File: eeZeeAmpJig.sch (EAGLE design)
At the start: 19 parts

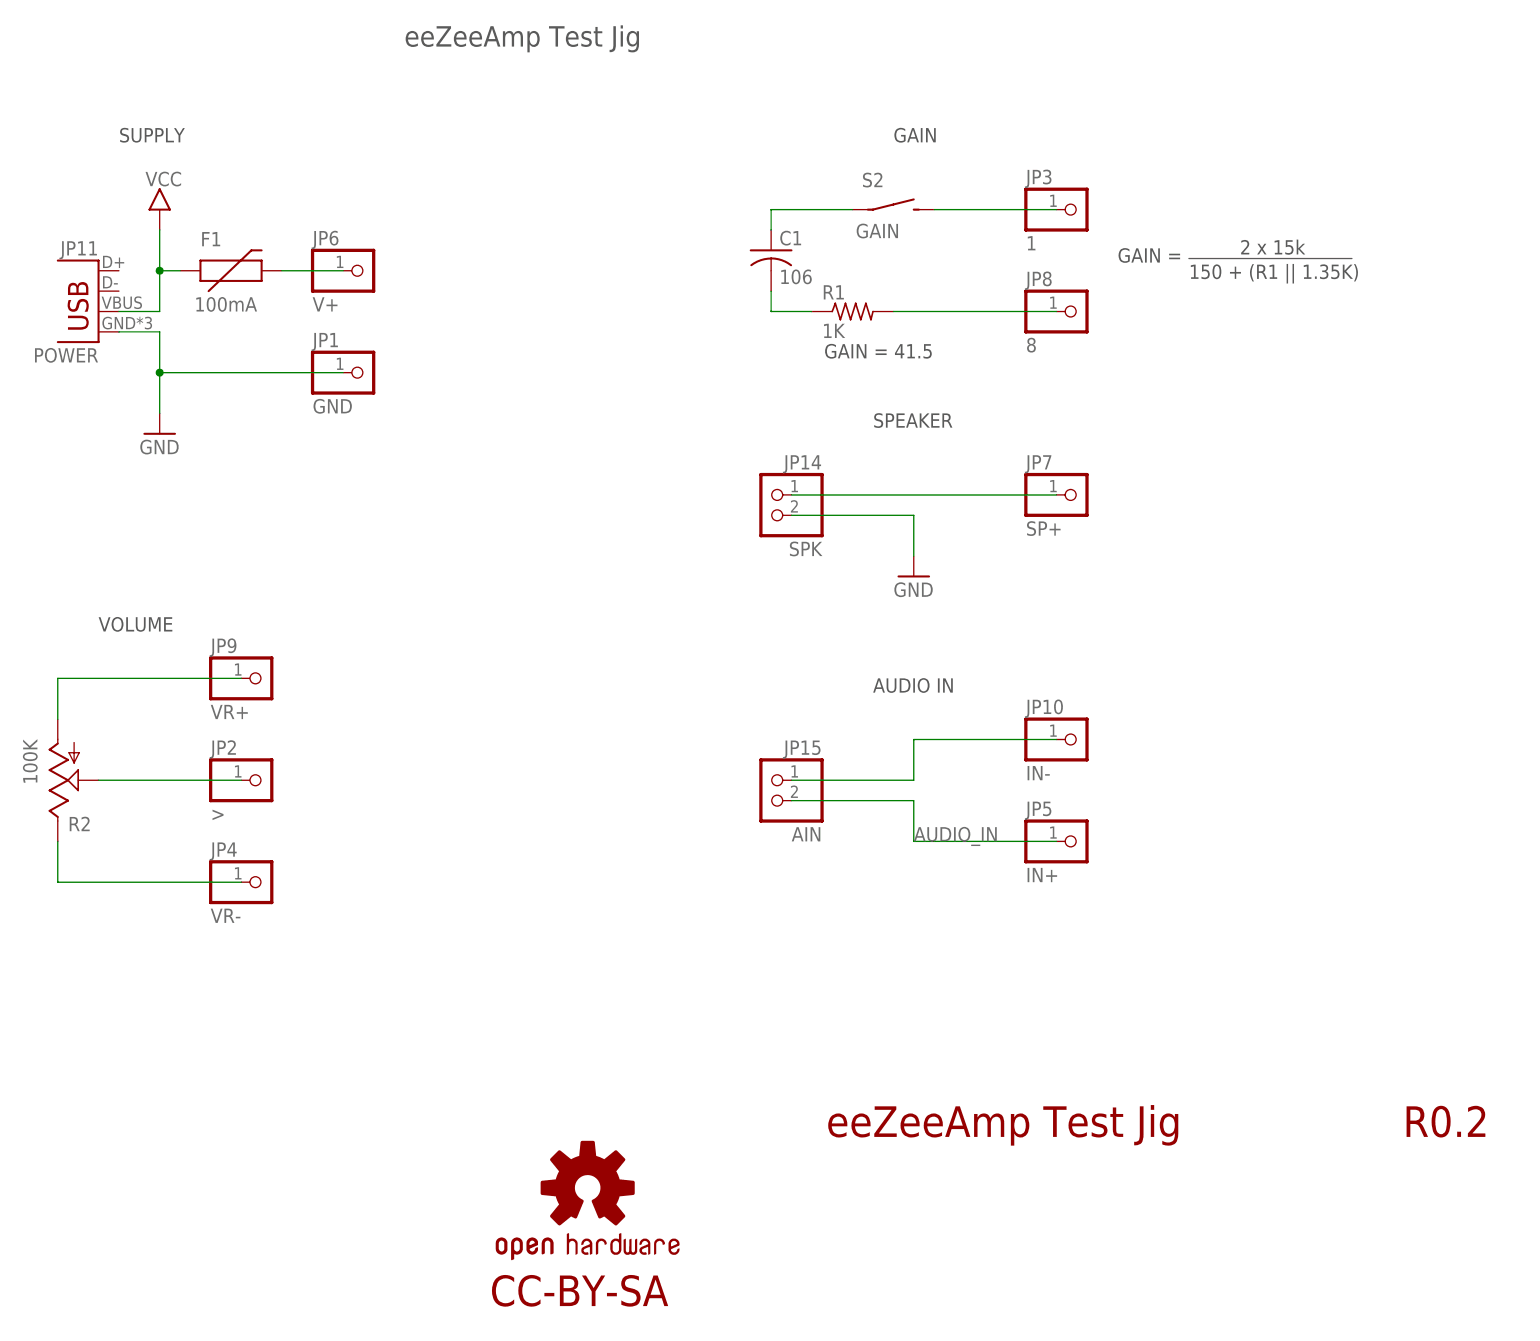
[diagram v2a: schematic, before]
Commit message: increased drill size for pogos, replaced microB with pin headers, moved power, ain, spkr pin headers, shrank board, centered pogo pin test area, reduced mounting hole drill size to #2, reduced spacer tdocu circles to actual for #2 size screws, changed switch to smaller smt version
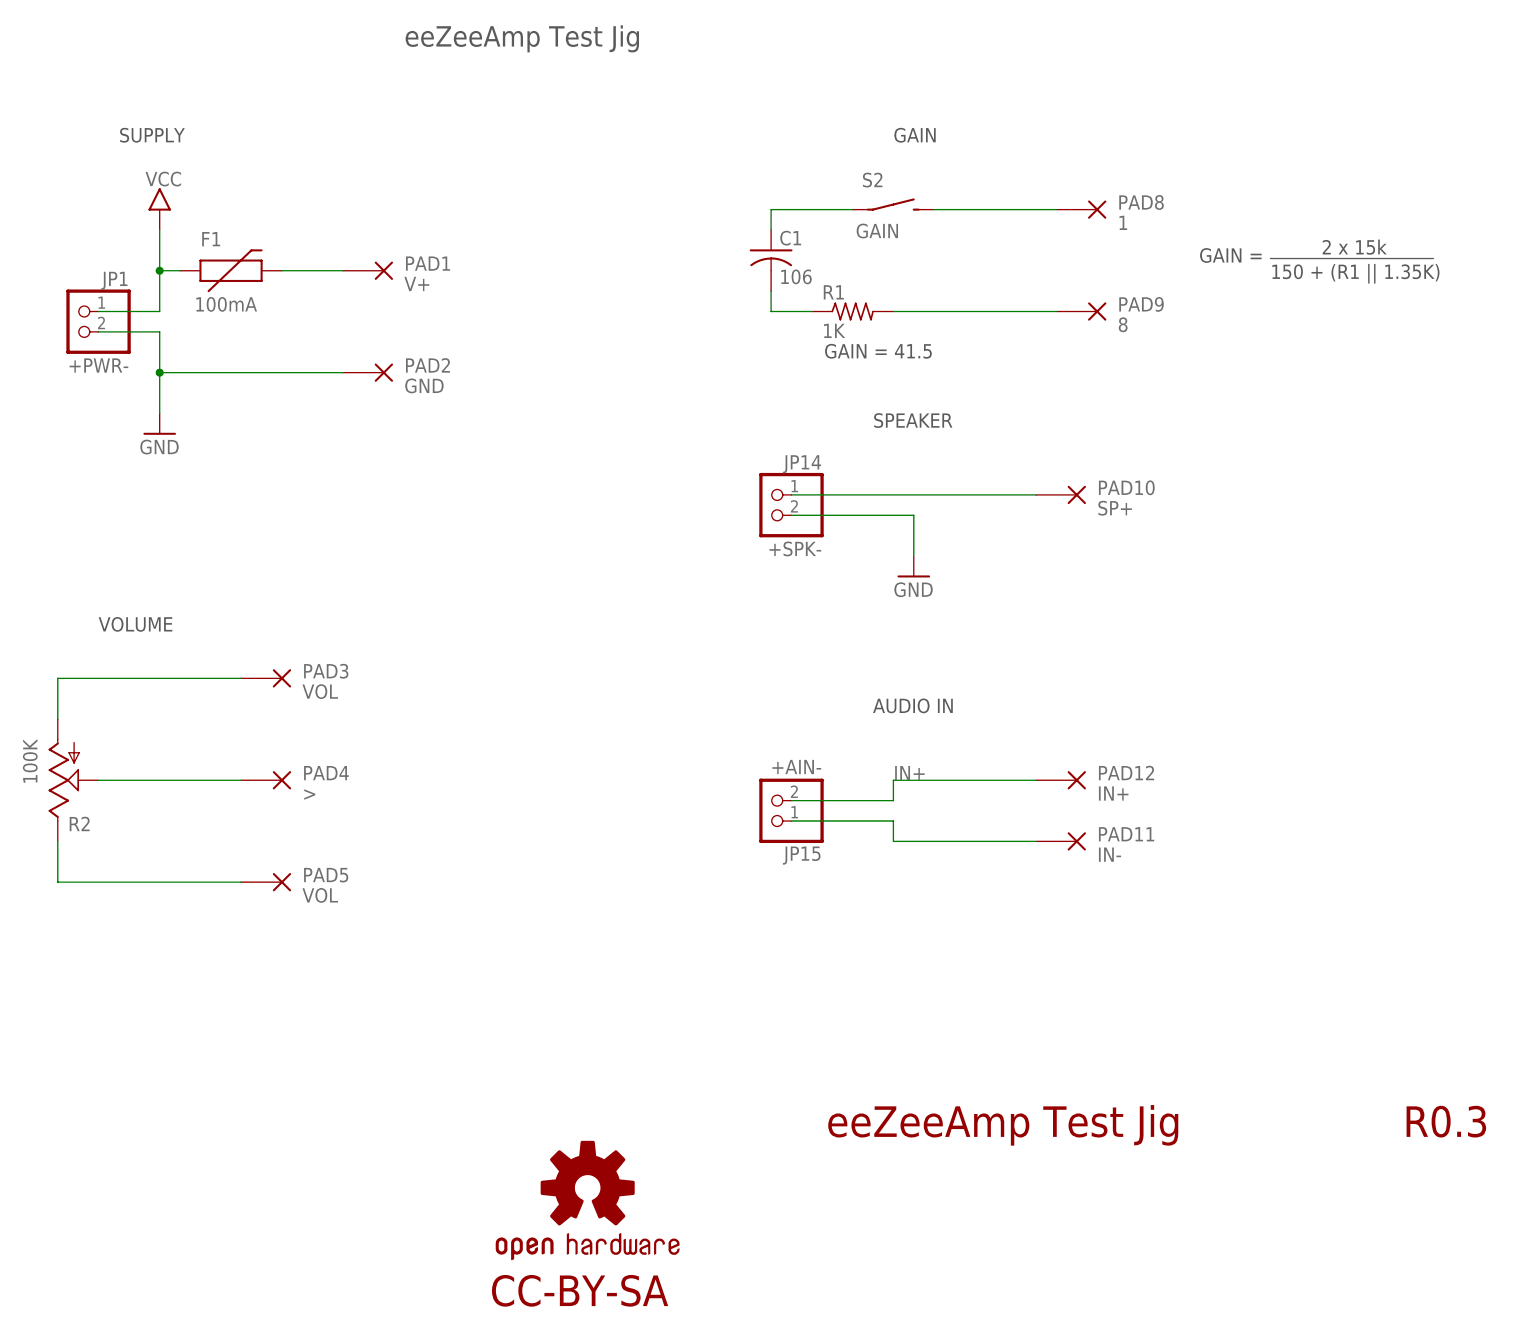
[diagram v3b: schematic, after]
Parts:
- removed JP10: IN-, pinhead-2:PINHD-1X01_2.54-S
- removed JP11: POWER, SparkFun-Connectors:USB-MICROB
- removed JP2: >, pinhead-2:PINHD-1X01_2.54-S
- removed JP3: 1, pinhead-2:PINHD-1X01_2.54-S
- removed JP4: VR-, pinhead-2:PINHD-1X01_2.54-S
- removed JP5: IN+, pinhead-2:PINHD-1X01_2.54-S
- removed JP6: V+, pinhead-2:PINHD-1X01_2.54-S
- removed JP7: SP+, pinhead-2:PINHD-1X01_2.54-S
- removed JP8: 8, pinhead-2:PINHD-1X01_2.54-S
- removed JP9: VR+, pinhead-2:PINHD-1X01_2.54-S
- added PAD1: V+, bt_electromech:WIREPAD_1.2MM
- added PAD10: SP+, bt_electromech:WIREPAD_1.2MM
- added PAD11: IN-, bt_electromech:WIREPAD_1.2MM
- added PAD12: IN+, bt_electromech:WIREPAD_1.2MM
- added PAD2: GND, bt_electromech:WIREPAD_1.2MM
- added PAD3, PAD5: VOL, bt_electromech:WIREPAD_1.2MM
- added PAD4: >, bt_electromech:WIREPAD_1.2MM
- added PAD8: 1, bt_electromech:WIREPAD_1.2MM
- added PAD9: 8, bt_electromech:WIREPAD_1.2MM
- C1: device rcl:C-USC1206 -> rcl:C-USC0805
- JP1: value GND -> +PWR-; device pinhead-2:PINHD-1X01_2.54-S -> pinhead-2:PINHD-1X02_2.54-S
- JP14: value SPK -> +SPK-
- JP15: value AIN -> +AIN-
- S2: device bt_electromech:SPST_TAC_RECT1 -> bt_electromech:SPST_3X4X2
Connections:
- removed net AUDIO_IN: JP15.2, JP5.1
- removed net N$2: JP10.1, JP15.1
- new net IN+: JP15.2, PAD12.P
- new net IN-: JP15.1, PAD11.P
- net 3: now also PAD4.P; no longer JP2.1
- net 8: now also PAD9.P; no longer JP8.1
- net GND: now also JP1.2, PAD2.P; no longer JP1.1, JP11.GND
- net N$1: now also PAD8.P; no longer JP3.1
- net N$3: now also PAD5.P; no longer JP4.1
- net N$4: now also PAD1.P; no longer JP6.1
- net N$8: now also PAD3.P; no longer JP9.1
- net SPEAKER: now also PAD10.P; no longer JP7.1
- net VCC: now also JP1.1; no longer JP11.VBUS
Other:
- note added: "R0.3"
- note removed: "R0.2"
- moved on the sheet: JP15
